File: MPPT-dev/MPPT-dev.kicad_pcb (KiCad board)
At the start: 2 copper layers, 29 parts, among them J1 200528-0100, J13 282834-6, J2 Conn_01x02, Q1 PMOS, U1 LTC4412xS6, U2 LT8611EUDD-PBF, U3 AD5245BRJZ10-R2

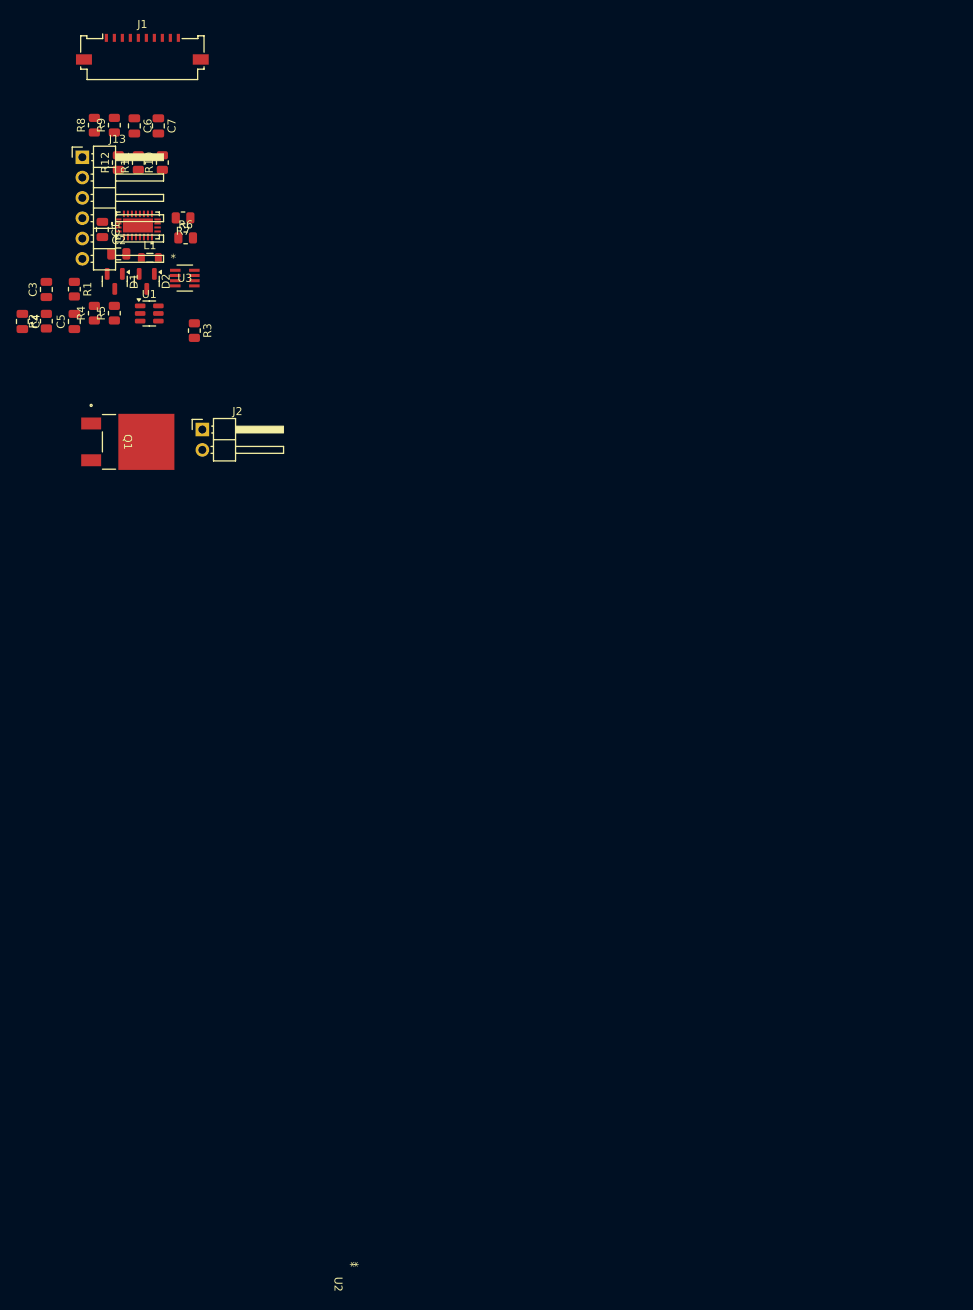
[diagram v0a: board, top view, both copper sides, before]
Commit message: 1 mppt layout
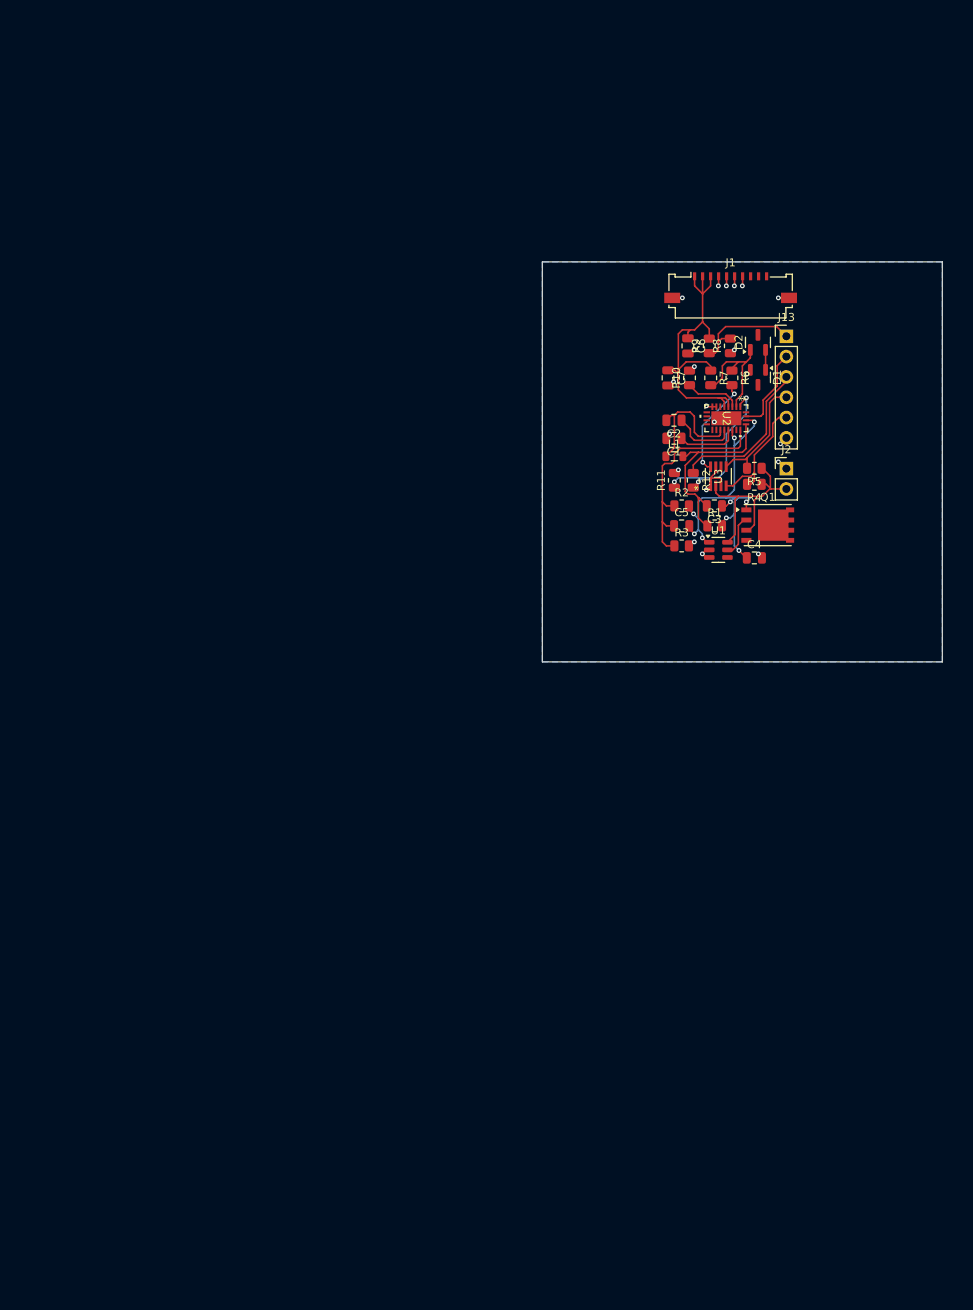
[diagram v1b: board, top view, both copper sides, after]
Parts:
- J13: footprint Connector_PinHeader_2.54mm:PinHeader_1x06_P2.54mm_Horizontal -> Connector_PinHeader_2.54mm:PinHeader_1x06_P2.54mm_Vertical
- J2: footprint Connector_PinHeader_2.54mm:PinHeader_1x02_P2.54mm_Horizontal -> Connector_PinHeader_2.54mm:PinHeader_1x02_P2.54mm_Vertical
- Q1: footprint footprints:TO252_DMP6180SK3_DIO -> Package_SO:PowerPAK_SO-8_Single
- moved C4 96.2 mm to (141.5, 112.0), turned to 0 degrees
- moved J13 90.8 mm to (145.5, 84.3)
- moved C3 87.8 mm to (136.5, 105.5), turned to 180 degrees
- moved R1 85.3 mm to (136.5, 108.0), turned to 0 degrees
- moved R4 85.2 mm to (141.5, 102.8), turned to 180 degrees
- moved R8 84.2 mm to (138.5, 85.5)
- moved R2 82.7 mm to (132.4, 105.5), turned to 0 degrees
- moved R5 82.3 mm to (141.5, 100.8), turned to 180 degrees
- moved R12 82.1 mm to (133.9, 102.3), turned to -90 degrees
- moved D1 81.3 mm to (141.9, 89.4)
- moved Q1 80.7 mm to (143.2, 107.9), turned to 0 degrees
- moved C5 80.1 mm to (132.4, 108.0), turned to 0 degrees
- moved J1 79.3 mm to (138.5, 77.7)
- moved R9 79.3 mm to (135.9, 85.5)
- moved R11 77.9 mm to (131.5, 102.3)
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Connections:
- J13 pad 1: /MODE -> /VIN_RD
- J13 pad 2: /VIN_RD -> /ICHG_RD
- J13 pad 3: /ICHG_RD -> /MODE
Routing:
- net /MPPT/BIAS: track 0.00 -> 45.2 mm, vias 0 -> 9
- net D_VSOLAR1: track 0.00 -> 41.0 mm
- net /MPPT/FB: track 0.00 -> 27.9 mm
- net GND: track 0.35 -> 27.1 mm, vias 0 -> 21
- net /BATTERY: track 0.00 -> 26.0 mm
- net /MPPT/ISP: track 0.00 -> 24.4 mm
- net /MPPT/SYNC: track 0.00 -> 21.5 mm, vias 0 -> 3
- net /MODE: track 0.00 -> 19.9 mm
- net /MPPT/SW1: track 0.00 -> 15.9 mm
- net /MPPT/MP_CTRL: track 0.00 -> 15.8 mm
- net /SCL: track 0.00 -> 15.5 mm
- net /SDA: track 0.00 -> 14.8 mm
- net /VIN_RD: track 0.00 -> 14.4 mm
- net /MPPT/A: track 0.00 -> 12.6 mm, vias 0 -> 2
- net /ICHG_RD: track 0.00 -> 10.6 mm
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- added copper zone on B.Cu, net GND
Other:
- board outline added: 50 x 50 mm

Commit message: Board review
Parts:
- removed J13: 282834-6, Connector_PinHeader_2.54mm:PinHeader_1x06_P2.54mm_Vertical
- removed Q1: PMOS, Package_SO:PowerPAK_SO-8_Single
- added C10: 10u, Capacitor_SMD:C_0603_1608Metric, F.Cu at (134.7, 109.7)
- added C8: 10u, Capacitor_SMD:C_0603_1608Metric, F.Cu at (134.7, 108.2)
- added C9: 10u, Capacitor_SMD:C_0603_1608Metric, F.Cu at (134.7, 111.2)
- added J3: Conn_01x07, Connector_PinHeader_2.54mm:PinHeader_1x07_P2.54mm_Vertical, F.Cu at (159.0, 83.3)
- added Q13: SIRA99DP-T1-GE3, Package_SO:PowerPAK_SO-8_Single, F.Cu at (140.7, 109.3)
- C1: value 1u -> 22u; footprint Capacitor_SMD:C_0805_2012Metric -> Capacitor_SMD:C_0603_1608Metric
- C2: value 0.1u -> 4u7; footprint Capacitor_SMD:C_0805_2012Metric -> Capacitor_SMD:C_0603_1608Metric
- C3: footprint Capacitor_SMD:C_0805_2012Metric -> Capacitor_SMD:C_0603_1608Metric
- C4: value 0.1u -> 100n; footprint Capacitor_SMD:C_0805_2012Metric -> Capacitor_SMD:C_0603_1608Metric
- C5: value 10p -> 1u; footprint Capacitor_SMD:C_0805_2012Metric -> Capacitor_SMD:C_0603_1608Metric
- C6: value 4.7u -> 10p; footprint Capacitor_SMD:C_0805_2012Metric -> Capacitor_SMD:C_0603_1608Metric
- C7: value 22u -> 10u; footprint Capacitor_SMD:C_0805_2012Metric -> Capacitor_SMD:C_0603_1608Metric
- J1: footprint Argus-Connectors:Molex_200528-0100_1x10-1MP_P1.00mm_Horizontal -> footprints:Molex_200528-0100_1x10-1MP_P1.00mm_Horizontal
- L1: value 4.7u -> 4u7; footprint Inductor_SMD:L_0805_2012Metric -> footprints:IND_03-4R7-R_EAT
- R1: value 50m -> 309k; footprint Resistor_SMD:R_0805_2012Metric -> Resistor_SMD:R_0603_1608Metric
- R10: value 60.4K -> 50m; footprint Resistor_SMD:R_0805_2012Metric -> Resistor_SMD:R_0603_1608Metric
- R11: value 0 -> 130k; footprint Resistor_SMD:R_0805_2012Metric -> Resistor_SMD:R_0603_1608Metric
- R12: value 0 -> 1M; footprint Resistor_SMD:R_0805_2012Metric -> Resistor_SMD:R_0603_1608Metric
- R2: value 1M -> 6k2; footprint Resistor_SMD:R_0805_2012Metric -> Resistor_SMD:R_0603_1608Metric
- R3: value 309K -> ?R; footprint Resistor_SMD:R_0805_2012Metric -> Resistor_SMD:R_0603_1608Metric
- R4: value 10K -> ?R; footprint Resistor_SMD:R_0805_2012Metric -> Resistor_SMD:R_0603_1608Metric
- R5: value 10K -> 10k; footprint Resistor_SMD:R_0805_2012Metric -> Resistor_SMD:R_0603_1608Metric
- R6: value 6.2K -> 10k; footprint Resistor_SMD:R_0805_2012Metric -> Resistor_SMD:R_0603_1608Metric
- R7: value 309K -> 60k4; footprint Resistor_SMD:R_0805_2012Metric -> Resistor_SMD:R_0603_1608Metric
- R8, R9: value R_Small -> 0R; footprint Resistor_SMD:R_0805_2012Metric -> Resistor_SMD:R_0603_1608Metric
- moved R3 29.4 mm to (154.2, 90.7), turned to 180 degrees
- moved U3 21.3 mm to (151.9, 86.6), turned to 180 degrees
- moved R2 21.1 mm to (146.3, 89.7), turned to 90 degrees
- moved R9 20.7 mm to (154.2, 95.2), turned to 0 degrees
- moved R5 20.1 mm to (150.7, 82.9), turned to -90 degrees
- moved R1 20.1 mm to (144.8, 89.7), turned to -90 degrees
- moved C5 20.0 mm to (147.1, 94.4), turned to -90 degrees
- moved C6 18.5 mm to (146.8, 98.0)
- moved R8 17.7 mm to (154.2, 93.7), turned to 180 degrees
- moved C7 17.7 mm to (134.7, 106.7), turned to 180 degrees
- moved R11 17.4 mm to (148.3, 98.0), turned to -90 degrees
- moved R4 16.5 mm to (154.2, 92.2), turned to 0 degrees
- moved J2 16.0 mm to (139.7, 115.8), turned to 90 degrees
- moved R6 15.8 mm to (153.1, 82.9)
- moved C1 15.4 mm to (141.7, 85.6)
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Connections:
- C1 pad 1: /MPPT/INTVcc -> /D_VSOLAR1
- C2 pad 1: /MPPT/BST -> /D_VSOLAR1
- C2 pad 2: /MPPT/SW1 -> GND
- C3 pad 1: /MPPT/BIAS -> /MPPT/INTVcc
- C3 pad 2: /MPPT/ISP -> GND
- C4 pad 1: /MPPT/BIAS -> /MPPT/BST
- C4 pad 2: GND -> /MPPT/SW
- C5 pad 1: /MPPT/FB -> /MPPT/BIAS
- C5 pad 2: /MPPT/BIAS -> /MPPT/ISP
- C6 pad 1: D_VSOLAR1 -> /MPPT/FB
- C6 pad 2: GND -> /MPPT/BIAS
- C7 pad 1: D_VSOLAR1 -> /MPPT/BIAS
- D1 pad 1: Net-(D2-A) -> /MPPT/MP_CTRL
- D1 pad 2: GND -> Net-(D1-A)
- D2 pad 1: /MPPT/MP_CTRL -> Net-(D1-A)
- D2 pad 2: Net-(D2-A) -> GND
- J1 pad 1: D_VSOLAR1 -> /D_VSOLAR1
- J1 pad 2: D_VSOLAR1 -> /D_VSOLAR1
- J1 pad 3: D_VSOLAR1 -> /D_VSOLAR1
- L1 pad 1: /MPPT/SW1 -> /MPPT/SW
- R1 pad 1: /MPPT/ISP -> /D_VSOLAR1
- R1 pad 2: /MPPT/BIAS -> /MPPT/MP_CTRL
- R10 pad 1: /MPPT/RT -> /MPPT/ISP
- R10 pad 2: GND -> /MPPT/BIAS
- R11 pad 1: /MPPT/SYNC -> /MPPT/FB
- R12 pad 1: /MODE -> /MPPT/FB
- R12 pad 2: /MPPT/SYNC -> /MPPT/BIAS
- R2 pad 1: /MPPT/FB -> /MPPT/MP_CTRL
- R2 pad 2: /MPPT/BIAS -> /MPPT/A
- R3 pad 1: /MPPT/FB -> /VIN_RD
- R3 pad 2: GND -> /D_VSOLAR1
- R4 pad 1: /BATTERY -> GND
- R4 pad 2: /SCL -> /VIN_RD
- R5 pad 1: /BATTERY -> +3V3
- R6 pad 1: /MPPT/MP_CTRL -> +3V3
- R6 pad 2: /MPPT/A -> /SCL
- R7 pad 1: D_VSOLAR1 -> /MPPT/RT
- R7 pad 2: /MPPT/MP_CTRL -> GND
- R8 pad 1: GND -> /MODE
- R8 pad 2: /VIN_RD -> /MPPT/SYNC
- R9 pad 1: /VIN_RD -> /MPPT/SYNC
- R9 pad 2: D_VSOLAR1 -> GND
- U2 pad 10: unconnected-(U2-NC-Pad10) -> GND
- U2 pad 11: unconnected-(U2-NC-Pad11) -> GND
- U2 pad 12: unconnected-(U2-NC-Pad12) -> GND
- U2 pad 13: unconnected-(U2-SW-Pad13) -> /MPPT/SW
- U2 pad 14: unconnected-(U2-SW-Pad14) -> /MPPT/SW
- U2 pad 15: /MPPT/SW1 -> /MPPT/SW
- U2 pad 4: D_VSOLAR1 -> /D_VSOLAR1
- U2 pad 5: D_VSOLAR1 -> /D_VSOLAR1
- U2 pad 6: unconnected-(U2-VIN-Pad6) -> /D_VSOLAR1
- U2 pad 9: unconnected-(U2-NC-Pad9) -> GND
- U3 pad 2: /BATTERY -> +3V3
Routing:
- net D_VSOLAR1: track 41.0 -> 0.00 mm
- net GND: track 27.1 -> 0.00 mm, vias 21 -> 52
- net /BATTERY: track 26.0 -> 0.00 mm
- net /MPPT/FB: track 27.9 -> 5.18 mm
- net +3V3: track 0.00 -> 16.6 mm, vias 0 -> 3
- net /MPPT/SW1: track 15.9 -> 0.00 mm
- net /MODE: track 19.9 -> 5.71 mm
- net /MPPT/SYNC: track 21.5 -> 11.9 mm, vias 3 -> 2
- net /D_VSOLAR1: track 0.00 -> 9.34 mm, vias 0 -> 2
- net /MPPT/MP_CTRL: track 15.8 -> 6.69 mm
- net /VIN_RD: track 14.4 -> 5.63 mm
- net /MPPT/A: track 12.6 -> 4.91 mm, vias 2 -> 0
- net /MPPT/BST: track 8.07 -> 2.13 mm
- net /ICHG_RD: track 10.6 -> 16.4 mm, vias 0 -> 1
- net /MPPT/INTVcc: track 7.69 -> 2.13 mm
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- added copper zone on F.Cu, net /BATTERY
- added copper zone on F.Cu, net /D_VSOLAR1
- added copper zone on F.Cu, net /MPPT/BIAS
- added copper zone on F.Cu, net /MPPT/ISP
- added copper zone on F.Cu, net /MPPT/SW
- added copper zone on F.Cu, net GND
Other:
- board size 50 x 50 mm -> 45.7 x 45.7 mm
- board text added: "+3V3"
- board text added: "BATT"
- board text added: "GND"
- board text added: "ICHG_RD"
- board text added: "LT8611 MPPT Controller ARGUS Cubesat v1.0"
- board text added: "MODE"
- board text added: "SCL"
- board text added: "SDA"
- board text added: "VIN_RD"
